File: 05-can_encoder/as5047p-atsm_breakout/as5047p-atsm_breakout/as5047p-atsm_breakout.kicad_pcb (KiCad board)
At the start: 2 copper layers, 25 x 25 mm, 8 parts, among them IC2 AS5047P-ATSM, J1 Conn_01x06

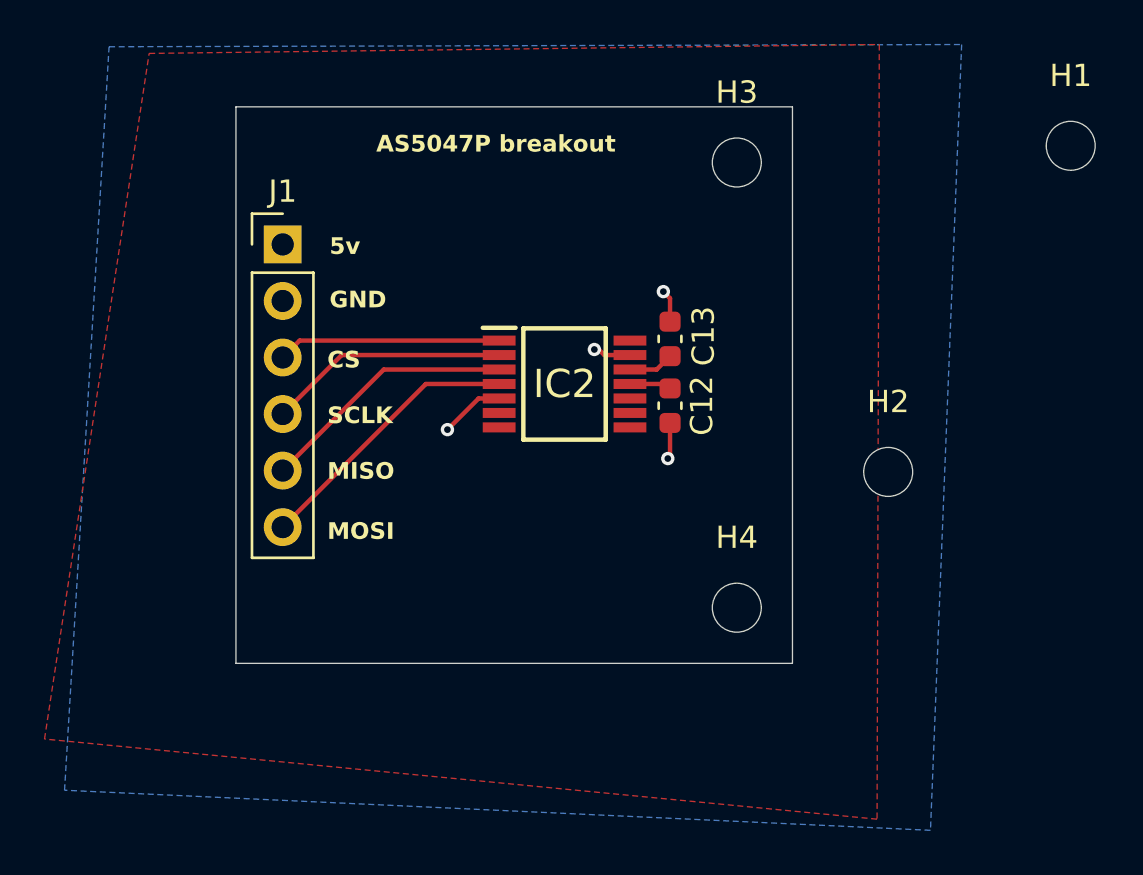
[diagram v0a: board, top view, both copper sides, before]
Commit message: stm and encoder breakout done/ordered
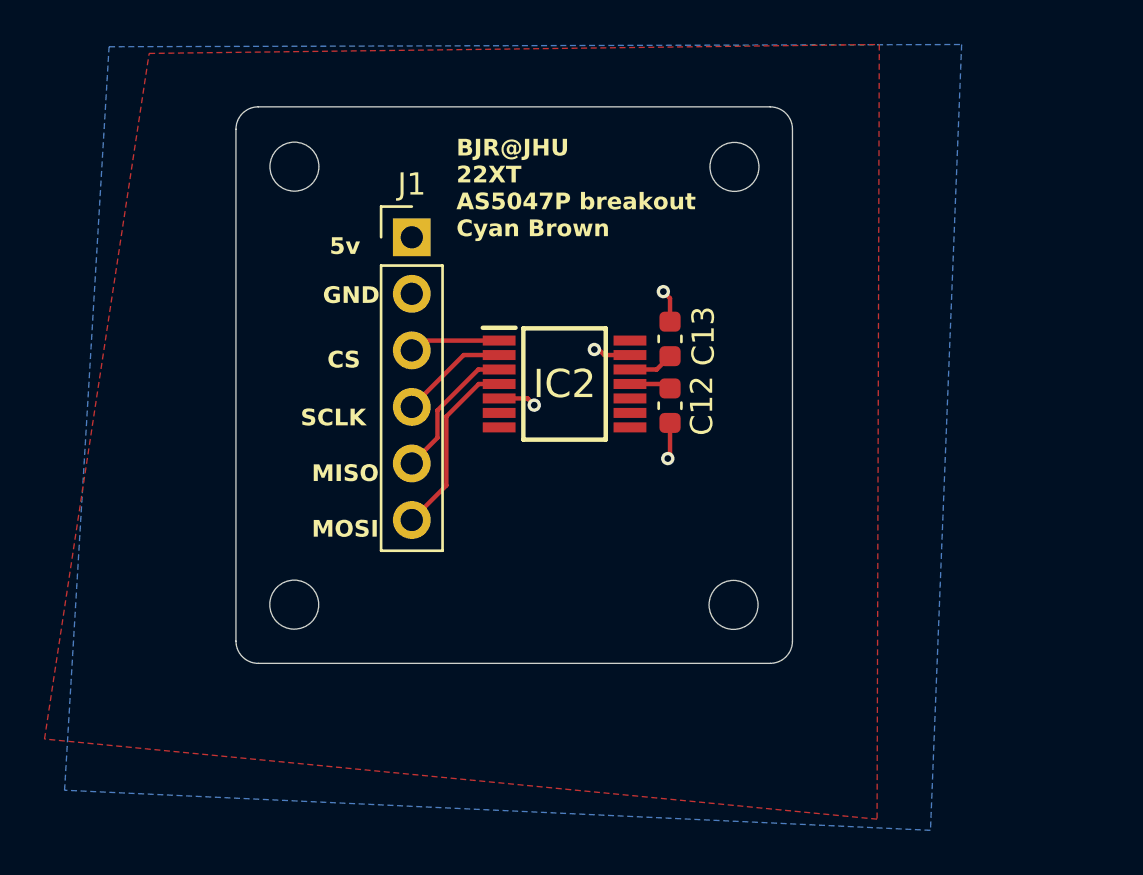
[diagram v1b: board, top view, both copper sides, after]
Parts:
- moved H2 27.3 mm to (132.7, 94.5)
- moved H3 19.9 mm to (132.7, 74.8)
- moved H1 15.1 mm to (152.5, 74.8)
- moved J1 5.81 mm to (138.0, 78.0)
- moved H4 0.19 mm to (152.5, 94.5)
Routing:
- net SCLK: track 10.8 -> 4.89 mm
- net !CS: track 10.0 -> 4.11 mm
- net MISO: track 11.6 -> 6.39 mm
- net MOSI: track 12.4 -> 8.27 mm
- net GND: track 7.72 -> 6.52 mm
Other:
- outline, holes or cut-outs redrawn
- board text added: "BJR@JHU 22XT AS5047P breakout Cyan Brown"
- board text removed: "AS5047P breakout"
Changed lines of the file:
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@@
 			(outputformat 1)
 			(mirror no)
-			(drillshape 1)
+			(drillshape 0)
 			(scaleselection 1)
-			(outputdirectory "")
+			(outputdirectory "gerbers/")
 		)
 	)
@@
 	(footprint "MountingHole:MountingHole_2.2mm_M2"
 		(layer "F.Cu")
-		(at 167.6 73.85)
+		(at 152.494313 74.79766)
 		(descr "Mounting Hole 2.2mm, M2, no annular, generated by kicad-footprint-generator mountinghole.py")
 		(tags "mountinghole M2")
@@
 			(at 0 -3.15 0)
 			(layer "F.SilkS")
+			(hide yes)
 			(effects
 				(font
@@
 	(footprint "MountingHole:MountingHole_2.2mm_M2"
 		(layer "F.Cu")
-		(at 152.6 94.6)
+		(at 152.453527 94.473245)
 		(descr "Mounting Hole 2.2mm, M2, no annular, generated by kicad-footprint-generator mountinghole.py")
 		(tags "mountinghole M2")
@@
 			(at 0 -3.15 0)
 			(layer "F.SilkS")
+			(hide yes)
 			(effects
 				(font
@@
 	(footprint "Connector_PinHeader_2.54mm:PinHeader_1x06_P2.54mm_Vertical"
 		(layer "F.Cu")
-		(at 132.2 78.28)
+		(at 138 77.96)
 		(descr "Through hole straight pin header, 1x06, 2.54mm pitch, single row")
 		(tags "Through hole pin header THT 1x06 2.54mm single row")
@@
 	(footprint "MountingHole:MountingHole_2.2mm_M2"
 		(layer "F.Cu")
-		(at 152.6 74.6)
+		(at 132.726625 74.786846)
 		(descr "Mounting Hole 2.2mm, M2, no annular, generated by kicad-footprint-generator mountinghole.py")
 		(tags "mountinghole M2")
@@
 			(at 0 -3.15 0)
 			(layer "F.SilkS")
+			(hide yes)
 			(effects
 				(font
@@
 	(footprint "MountingHole:MountingHole_2.2mm_M2"
 		(layer "F.Cu")
-		(at 159.4 88.5)
+		(at 132.718281 94.462431)
 		(descr "Mounting Hole 2.2mm, M2, no annular, generated by kicad-footprint-generator mountinghole.py")
 		(tags "mountinghole M2")
@@
 			(at 0 -3.15 0)
 			(layer "F.SilkS")
+			(hide yes)
 			(effects
 				(font
@@
 	)
 	(gr_line
-		(start 130.1 72.1)
-		(end 130.1 97.1)
+		(start 130.1 73.1)
+		(end 130.1 96.1)
 		(stroke
 			(width 0.05)
@@
 	)
 	(gr_line
-		(start 155.1 97.1)
-		(end 130.1 97.1)
+		(start 154.1 97.1)
+		(end 131.1 97.1)
 		(stroke
 			(width 0.05)
@@
 	)
 	(gr_line
-		(start 155.1 72.1)
-		(end 155.1 97.1)
+		(start 155.1 73.1)
+		(end 155.1 96.1)
 		(stroke
 			(width 0.05)
@@
 		(layer "Edge.Cuts")
 	)
-	(gr_line
-		(start 130.1 72.1)
-		(end 155.1 72.1)
+	(gr_arc
+		(start 154.1 72.1)
+		(mid 154.807107 72.392893)
+		(end 155.1 73.1)
 		(stroke
 			(width 0.05)
@@
 		(layer "Edge.Cuts")
 	)
+	(gr_arc
+		(start 130.1 73.1)
+		(mid 130.392893 72.392893)
+		(end 131.1 72.1)
+		(stroke
+			(width 0.05)
+			(type default)
+		)
+		(layer "Edge.Cuts")
+	)
+	(gr_arc
+		(start 155.1 96.1)
+		(mid 154.807107 96.807107)
+		(end 154.1 97.1)
+		(stroke
+			(width 0.05)
+			(type default)
+		)
+		(layer "Edge.Cuts")
+	)
+	(gr_line
+		(start 131.1 72.1)
+		(end 154.1 72.1)
+		(stroke
+			(width 0.05)
+			(type default)
+		)
+		(layer "Edge.Cuts")
+	)
+	(gr_arc
+		(start 131.1 97.1)
+		(mid 130.392893 96.807107)
+		(end 130.1 96.1)
+		(stroke
+			(width 0.05)
+			(type default)
+		)
+		(layer "Edge.Cuts")
+	)
 	(gr_text "GND"
-		(at 134.3 81.2 0)
+		(at 134 81 0)
 		(layer "F.SilkS")
 		(effects
@@
 	)
 	(gr_text "MOSI"
-		(at 134.2 91.6 0)
+		(at 133.5 91.5 0)
 		(layer "F.SilkS")
 		(effects
@@
 	)
 	(gr_text "SCLK"
-		(at 134.2 86.4 0)
+		(at 133 86.5 0)
 		(layer "F.SilkS")
 		(effects
@@
 		)
 	)
-	(gr_text "AS5047P breakout"
-		(at 136.4 74.2 0)
+	(gr_text "BJR@JHU\n22XT\nAS5047P breakout\nCyan Brown"
+		(at 140 78 0)
 		(layer "F.SilkS")
 		(effects
@@
 	)
 	(gr_text "MISO"
-		(at 134.2 88.9 0)
+		(at 133.5 89 0)
 		(layer "F.SilkS")
 		(effects
@@
 	)
 	(segment
+		(start 143.2 85.2)
+		(end 143.5 85.5)
+		(width 0.2)
+		(layer "F.Cu")
+		(net 1)
+	)
+	(segment
 		(start 146.4 83)
 		(end 146.65 83.25)
@@
 	)
 	(segment
-		(start 141 85.2)
-		(end 139.6 86.6)
-		(width 0.2)
-		(layer "F.Cu")
-		(net 1)
-	)
-	(segment
 		(start 141.924 85.2)
-		(end 141 85.2)
+		(end 143.2 85.2)
 		(width 0.2)
 		(layer "F.Cu")
@@
 	)
 	(via
-		(at 139.6 86.6)
+		(at 143.5 85.5)
 		(size 0.6)
 		(drill 0.3)
@@
 	)
 	(segment
+		(start 139.151 86.969)
+		(end 138 88.12)
+		(width 0.2)
+		(layer "F.Cu")
+		(net 5)
+	)
+	(segment
+		(start 139.151 85.7355)
+		(end 139.151 86.969)
+		(width 0.2)
+		(layer "F.Cu")
+		(net 5)
+	)
+	(segment
 		(start 141.924 83.9)
-		(end 136.74 83.9)
+		(end 140.9865 83.9)
 		(width 0.2)
 		(layer "F.Cu")
@@
 	)
 	(segment
-		(start 136.74 83.9)
-		(end 132.2 88.44)
+		(start 140.9865 83.9)
+		(end 139.151 85.7355)
 		(width 0.2)
 		(layer "F.Cu")
@@
 	)
 	(segment
-		(start 141.924 82.6)
-		(end 132.96 82.6)
+		(start 138.44 82.6)
+		(end 141.924 82.6)
 		(width 0.2)
 		(layer "F.Cu")
@@
 	)
 	(segment
-		(start 132.96 82.6)
-		(end 132.2 83.36)
+		(start 138 83.04)
+		(end 138.44 82.6)
 		(width 0.2)
 		(layer "F.Cu")
@@
 	)
 	(segment
-		(start 141.924 83.25)
-		(end 134.85 83.25)
+		(start 138 85.58)
+		(end 140.33 83.25)
 		(width 0.2)
 		(layer "F.Cu")
@@
 	)
 	(segment
-		(start 134.85 83.25)
-		(end 132.2 85.9)
+		(start 140.33 83.25)
+		(end 141.924 83.25)
 		(width 0.2)
 		(layer "F.Cu")
@@
 	)
 	(segment
-		(start 138.63 84.55)
-		(end 132.2 90.98)
+		(start 141.924 84.55)
+		(end 141.0095 84.55)
 		(width 0.2)
 		(layer "F.Cu")
@@
 	)
 	(segment
-		(start 141.924 84.55)
-		(end 138.63 84.55)
-		(width 0.2)
-		(layer "F.Cu")
+		(start 141.0095 84.55)
+		(end 139.552 86.0075)
+		(width 0.2)
+		(layer "F.Cu")
+		(net 9)
+	)
+	(segment
+		(start 139.552 86.0075)
+		(end 139.552 89.108)
+		(width 0.2)
+		(layer "F.Cu")
+		(net 9)
+	)
+	(segment
+		(start 139.552 89.108)
+		(end 138 90.66)
+		(width 0.2)
+		(layer "F.Cu")
